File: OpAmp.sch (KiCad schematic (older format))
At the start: 45 parts, among them J1 Conn_01x07, J2 Conn_01x02, J3 Conn_01x02, Q1 5551, Q10 5401, Q11 5551, Q12 TIP42, Q13 5551, Q14 5401, Q15 5551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

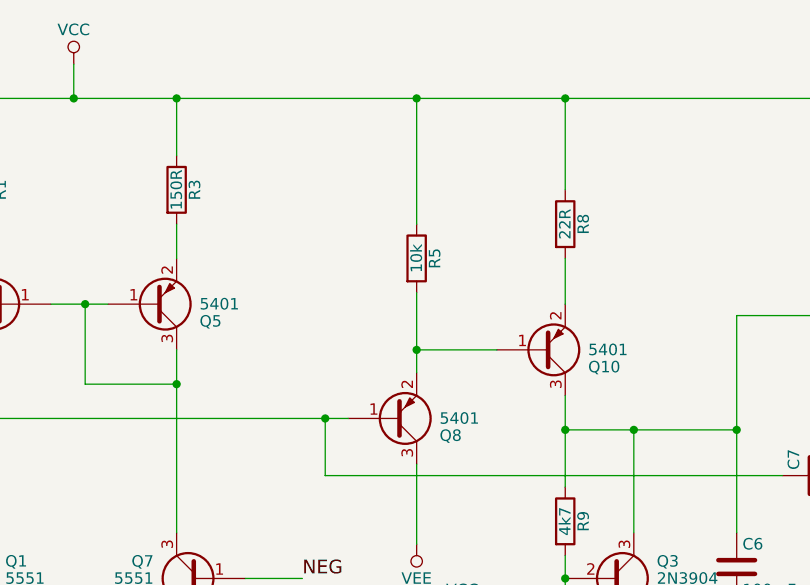
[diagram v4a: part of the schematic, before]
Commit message: Added VAS safety transistor
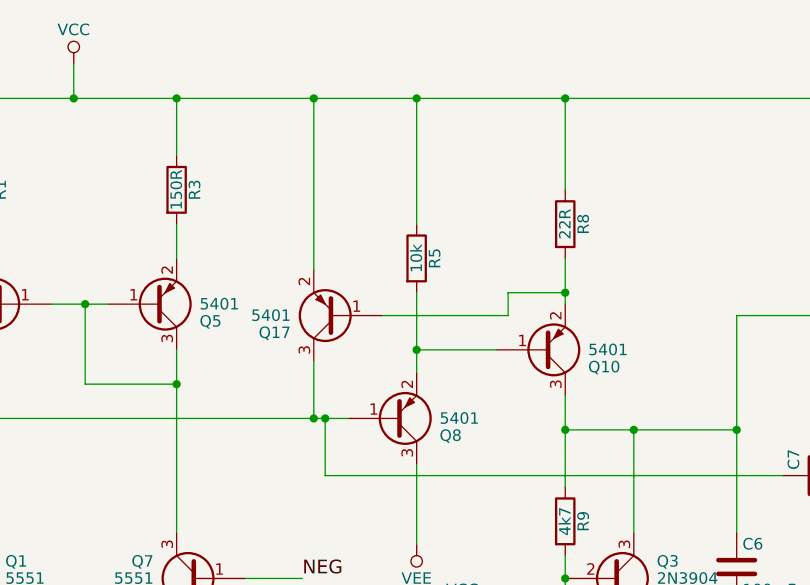
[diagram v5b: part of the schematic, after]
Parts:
- added Q17: 5401, TO_SOT_Packages_SMD:SOT-23, symbol MMBT3906
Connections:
- net VCC: now also Q17.2 (E)
- net at C7.1, Q1.3 (C), Q2.3 (C)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: now also Q17.3 (C)
- net at Q10.2 (E), R8.2: now also Q17.1 (B)
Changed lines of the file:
@@
 $EndComp
 $Comp
-L VCC #PWR01
+L VCC #PWR2
 U 1 1 6064E2D7
 P 1050 4300
-F 0 "#PWR01" H 1050 4150 50  0001 C CNN
+F 0 "#PWR2" H 1050 4150 50  0001 C CNN
 F 1 "VCC" H 1050 4450 50  0000 C CNN
 F 2 "" H 1050 4300 50  0001 C CNN
@@
 $EndComp
 $Comp
-L VEE #PWR02
+L VEE #PWR1
 U 1 1 6064E2F5
 P 1050 3900
-F 0 "#PWR02" H 1050 3750 50  0001 C CNN
+F 0 "#PWR1" H 1050 3750 50  0001 C CNN
 F 1 "VEE" H 1050 4050 50  0000 C CNN
 F 2 "" H 1050 3900 50  0001 C CNN
@@
 $EndComp
 $Comp
-L VCC #PWR03
+L VCC #PWR6
 U 1 1 6064EEAE
 P 2800 750
-F 0 "#PWR03" H 2800 600 50  0001 C CNN
+F 0 "#PWR6" H 2800 600 50  0001 C CNN
 F 1 "VCC" H 2800 900 50  0000 C CNN
 F 2 "" H 2800 750 50  0001 C CNN
@@
 $EndComp
 $Comp
-L VEE #PWR04
+L VEE #PWR7
 U 1 1 6064F415
 P 2850 5100
-F 0 "#PWR04" H 2850 4950 50  0001 C CNN
+F 0 "#PWR7" H 2850 4950 50  0001 C CNN
 F 1 "VEE" H 2850 5250 50  0000 C CNN
 F 2 "" H 2850 5100 50  0001 C CNN
@@
 $EndComp
 $Comp
-L VCC #PWR05
+L VCC #PWR9
 U 1 1 6065149D
 P 4500 3200
-F 0 "#PWR05" H 4500 3050 50  0001 C CNN
+F 0 "#PWR9" H 4500 3050 50  0001 C CNN
 F 1 "VCC" H 4500 3350 50  0000 C CNN
 F 2 "" H 4500 3200 50  0001 C CNN
@@
 $EndComp
 $Comp
-L VEE #PWR06
+L VEE #PWR8
 U 1 1 606515F7
 P 4300 2850
-F 0 "#PWR06" H 4300 2700 50  0001 C CNN
+F 0 "#PWR8" H 4300 2700 50  0001 C CNN
 F 1 "VEE" H 4300 3000 50  0000 C CNN
 F 2 "" H 4300 2850 50  0001 C CNN
@@
 $EndComp
 $Comp
-L VEE #PWR07
+L VEE #PWR5
 U 1 1 60654F68
 P 1750 2550
-F 0 "#PWR07" H 1750 2400 50  0001 C CNN
+F 0 "#PWR5" H 1750 2400 50  0001 C CNN
 F 1 "VEE" H 1750 2700 50  0000 C CNN
 F 2 "" H 1750 2550 50  0001 C CNN
@@
 $EndComp
 $Comp
-L VEE #PWR08
+L VEE #PWR3
 U 1 1 60657BCF
 P 1250 4800
-F 0 "#PWR08" H 1250 4650 50  0001 C CNN
+F 0 "#PWR3" H 1250 4650 50  0001 C CNN
 F 1 "VEE" H 1250 4950 50  0000 C CNN
 F 2 "" H 1250 4800 50  0001 C CNN
@@
 $EndComp
 $Comp
-L VCC #PWR09
+L VCC #PWR4
 U 1 1 60657EDE
 P 1250 5200
-F 0 "#PWR09" H 1250 5050 50  0001 C CNN
+F 0 "#PWR4" H 1250 5050 50  0001 C CNN
 F 1 "VCC" H 1250 5350 50  0000 C CNN
 F 2 "" H 1250 5200 50  0001 C CNN
@@
 	6950 4050 6950 3700
 Connection ~ 6950 3700
+$Comp
+L MMBT3906 Q17
+U 1 1 63BCF5A5
+P 3950 1850
+F 0 "Q17" H 4150 1925 50  0000 L CNN
+F 1 "5401" H 4150 1850 50  0000 L CNN
+F 2 "TO_SOT_Packages_SMD:SOT-23" H 4150 1775 50  0001 L CIN
+F 3 "" H 3950 1850 50  0001 L CNN
+F 4 "C8326" H 3950 1850 60  0001 C CNN "LCSC"
+	1    3950 1850
+	-1   0    0    1
+$EndComp
+Wire Wire Line
+	3850 2050 3850 2300
+Connection ~ 3850 2300
+Wire Wire Line
+	3850 1650 3850 900
+Connection ~ 3850 900
+Wire Wire Line
+	4150 1850 4700 1850
+Wire Wire Line
+	4700 1850 4700 1750
+Wire Wire Line
+	4700 1750 4950 1750
+Connection ~ 4950 1750
 $EndSCHEMATC

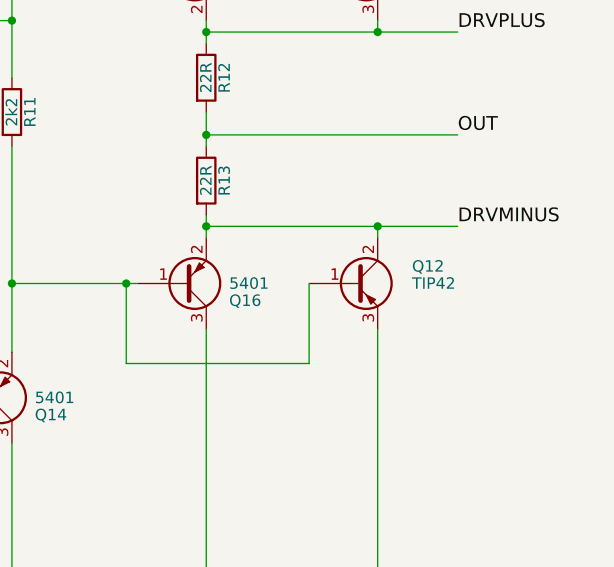
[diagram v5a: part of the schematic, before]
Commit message: Fixed pinout on TIP42
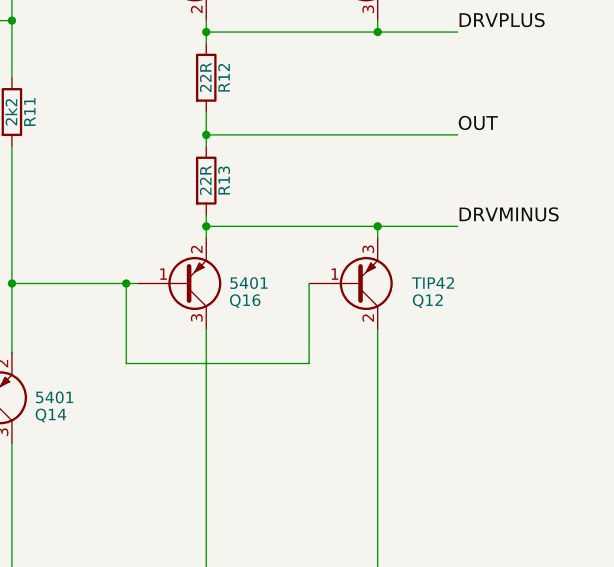
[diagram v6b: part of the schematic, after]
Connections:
- net DRVMINUS: now also Q12.3 (E); no longer Q12.2 (C)
- net VEE: now also Q12.2 (C); no longer Q12.3 (E)
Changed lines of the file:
@@
 F 3 "" H 7950 3700 50  0001 L CNN
 	1    7950 3700
-	1    0    0    -1
+	1    0    0    1
 $EndComp
 Wire Wire Line
